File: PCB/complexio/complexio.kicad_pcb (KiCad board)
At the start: 2 copper layers, 1 part, among them U1 STM32F401RETx

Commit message: Initial code,schem & added assets
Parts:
- added BL1: Bluetooth HC-05 module, Connector_PinSocket_2.54mm:PinSocket_1x06_P2.54mm_Vertical, F.Cu at (104.8, 77.9)
- added C1: 100n, Capacitor_SMD:C_0402_1005Metric, F.Cu at (108.5, 76.6)
- added C10: 10u, Capacitor_SMD:C_0603_1608Metric, F.Cu at (128.7, 175.1)
- added C11: 100n, Capacitor_SMD:C_0402_1005Metric, F.Cu at (124.0, 178.5)
- added C12: 1u, Capacitor_SMD:C_0402_1005Metric, F.Cu at (125.9, 178.5)
- added C13: 100n, Capacitor_SMD:C_0402_1005Metric, F.Cu at (127.9, 178.5)
- added C14: 1u, Capacitor_SMD:C_0402_1005Metric, F.Cu at (129.9, 178.5)
- added C15: 100n, Capacitor_SMD:C_0402_1005Metric, F.Cu at (131.8, 178.5)
- added C16: 1u, Capacitor_SMD:C_0402_1005Metric, F.Cu at (133.8, 178.5)
- added C2: 100n, Capacitor_SMD:C_0402_1005Metric, F.Cu at (108.5, 78.6)
- added C3: 100n, Capacitor_SMD:C_0402_1005Metric, F.Cu at (108.5, 80.5)
- added C4: 100n, Capacitor_SMD:C_0402_1005Metric, F.Cu at (108.5, 82.5)
- added C5: 10u, Capacitor_SMD:C_0603_1608Metric, F.Cu at (112.0, 88.2)
- added C6: 10n, Capacitor_SMD:C_0402_1005Metric, F.Cu at (108.5, 84.5)
- added C7: 1u, Capacitor_SMD:C_0402_1005Metric, F.Cu at (108.5, 86.5)
- added C8: 1u, Capacitor_SMD:C_0402_1005Metric, F.Cu at (108.5, 88.4)
- added C9: 100n, Capacitor_SMD:C_0402_1005Metric, F.Cu at (108.5, 90.4)
- added FB1: 120R, Inductor_SMD:L_0603_1608Metric, F.Cu at (112.0, 90.7)
- added IMU1: MPU6050, MPU6050:MPU6050, F.Cu at (89.6, 58.2)
- added J3: Conn_01x12_Pin, Connector_PinHeader_2.54mm:PinHeader_1x12_P2.54mm_Horizontal, F.Cu at (107.4, 147.0)
- added OLED1: SPI OLED Screen 128x64 pixels, Connector_PinSocket_2.54mm:PinSocket_1x07_P2.54mm_Vertical, F.Cu at (104.8, 58.1)
- added Q1: AO3400A, Package_TO_SOT_SMD:SOT-23, F.Cu at (125.2, 174.6)
- added R1: 10k, Resistor_SMD:R_0402_1005Metric, F.Cu at (115.4, 88.0)
- added R10: 47k, Resistor_SMD:R_0402_1005Metric, F.Cu at (116.0, 175.6)
- added R11: 47k, Resistor_SMD:R_0402_1005Metric, F.Cu at (118.0, 175.6)
- added R12: 47, Resistor_SMD:R_0402_1005Metric, F.Cu at (120.0, 175.6)
- added R13: 47, Resistor_SMD:R_0402_1005Metric, F.Cu at (122.0, 175.6)
- added R14: 47k, Resistor_SMD:R_0402_1005Metric, F.Cu at (112.0, 172.7)
- added R15: 47k, Resistor_SMD:R_0402_1005Metric, F.Cu at (114.0, 172.7)
- added R16: 47, Resistor_SMD:R_0402_1005Metric, F.Cu at (116.0, 172.7)
- added R2: 47k, Resistor_SMD:R_0402_1005Metric, F.Cu at (112.0, 178.5)
- added R3: 47k, Resistor_SMD:R_0402_1005Metric, F.Cu at (114.0, 178.5)
- added R4: 47k, Resistor_SMD:R_0402_1005Metric, F.Cu at (116.0, 178.5)
- added R5: 47, Resistor_SMD:R_0402_1005Metric, F.Cu at (118.0, 178.5)
- added R6: 47k, Resistor_SMD:R_0402_1005Metric, F.Cu at (120.0, 178.5)
- added R7: 47k, Resistor_SMD:R_0402_1005Metric, F.Cu at (122.0, 178.5)
- added R8: 47, Resistor_SMD:R_0402_1005Metric, F.Cu at (112.0, 175.6)
- added R9: 47k, Resistor_SMD:R_0402_1005Metric, F.Cu at (114.0, 175.6)
- added SW1: SW_SPDT, Button_Switch_THT:SW_E-Switch_EG1224_SPDT_Angled, F.Cu at (110.9, 59.4)
- added U10: KTIR0711S, KTIR0711S:KTIR0711S, F.Cu at (114.2, 163.9)
- added U11: KTIR0711S, KTIR0711S:KTIR0711S, F.Cu at (119.1, 163.9)
- added U12: KTIR0711S, KTIR0711S:KTIR0711S, F.Cu at (124.0, 163.9)
- added U2: TB6612FNG, Package_SO:SSOP-24_5.3x8.2mm_P0.65mm, F.Cu at (97.2, 60.8)
- added U3: TB6612FNG, Package_SO:SSOP-24_5.3x8.2mm_P0.65mm, F.Cu at (97.2, 70.8)
- added U4: KTIR0711S, KTIR0711S:KTIR0711S, F.Cu at (114.2, 152.1)
- added U5: KTIR0711S, KTIR0711S:KTIR0711S, F.Cu at (119.1, 152.1)
- added U6: KTIR0711S, KTIR0711S:KTIR0711S, F.Cu at (124.0, 152.1)
- added U7: KTIR0711S, KTIR0711S:KTIR0711S, F.Cu at (114.2, 158.0)
- added U8: KTIR0711S, KTIR0711S:KTIR0711S, F.Cu at (119.1, 158.0)
- added U9: KTIR0711S, KTIR0711S:KTIR0711S, F.Cu at (124.0, 158.0)
- U1: value STM32F401RETx -> STM32F103C8T6; footprint Package_QFP:LQFP-64_10x10mm_P0.5mm -> Package_QFP:LQFP-48_7x7mm_P0.5mm
- moved U1 30.1 mm to (115.6, 81.3)
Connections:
- U1 pad 1: unconnected-(U1-VBAT-Pad1) -> +3V3
- U1 pad 18: Net-(U1-VSS-Pad18) -> unconnected-(U1-PB0-Pad18)
- U1 pad 23: unconnected-(U1-PA7-Pad23) -> GND
- U1 pad 24: unconnected-(U1-PC4-Pad24) -> +3V3
- U1 pad 31: Net-(U1-VSS-Pad18) -> unconnected-(U1-PA10-Pad31)
- U1 pad 35: unconnected-(U1-PB14-Pad35) -> GND
- U1 pad 36: unconnected-(U1-PB15-Pad36) -> +3V3
- U1 pad 44: unconnected-(U1-PA11-Pad44) -> /BOOT0
- U1 pad 47: Net-(U1-VSS-Pad18) -> GND
- U1 pad 48: unconnected-(U1-VDD-Pad48) -> +3V3
- U1 pad 7: unconnected-(U1-NRST-Pad7) -> /NRST
- U1 pad 8: unconnected-(U1-PC0-Pad8) -> GND
- U1 pad 9: unconnected-(U1-PC1-Pad9) -> +3.3VA
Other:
- board outline added: 69 x 130 mm

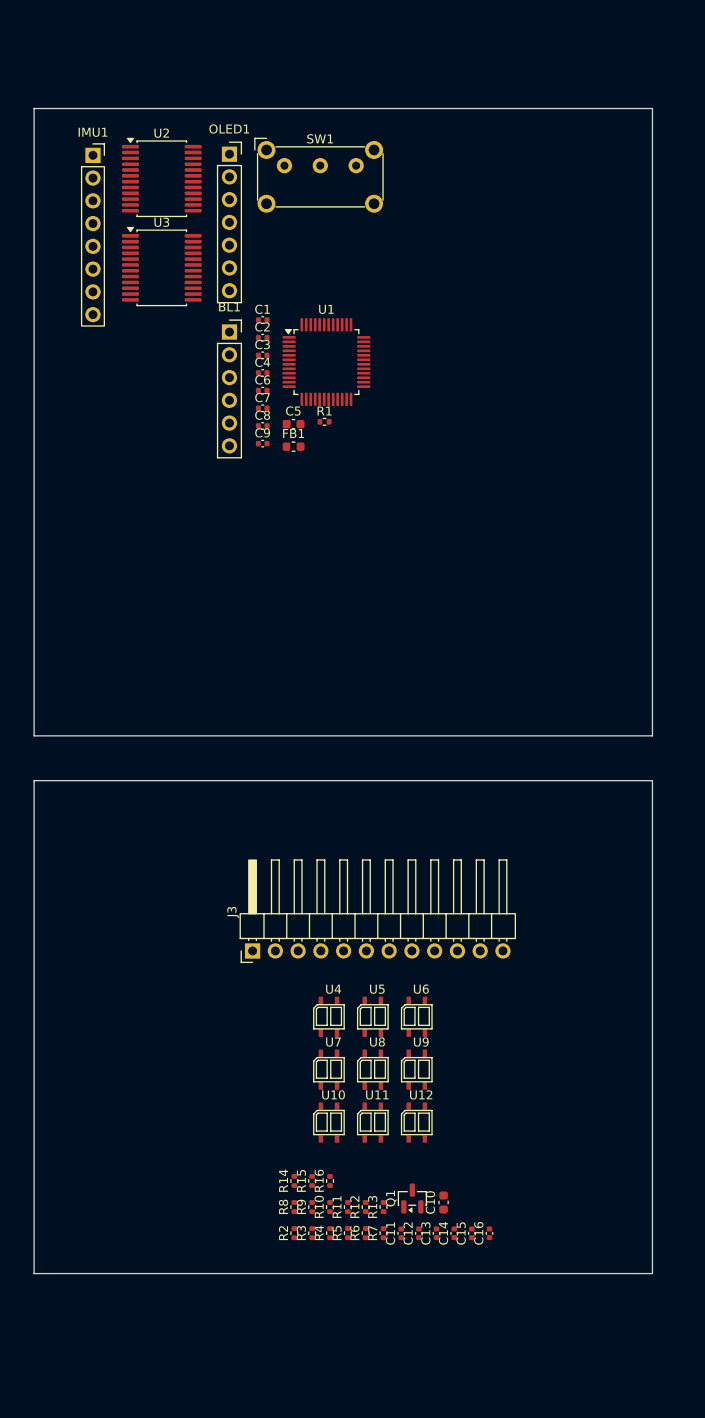
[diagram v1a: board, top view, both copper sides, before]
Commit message: Sensor array finished & main schem modified
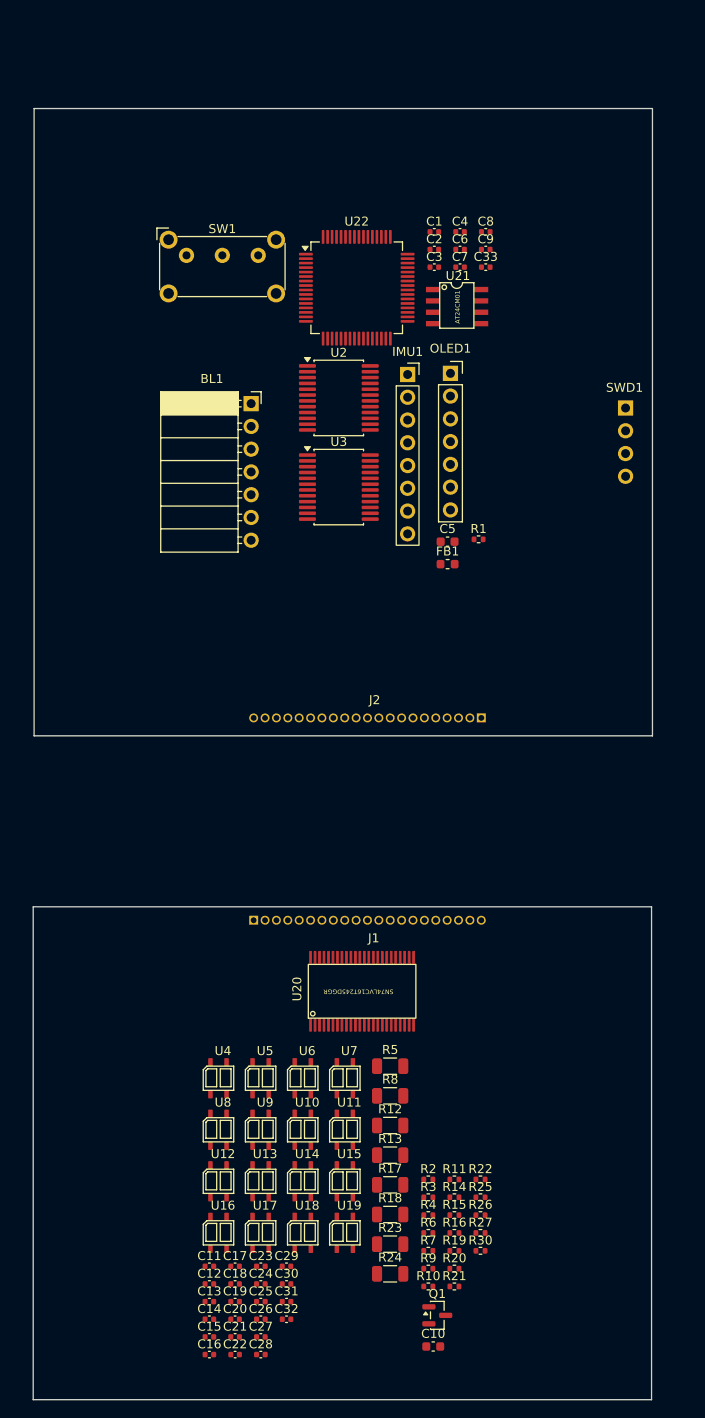
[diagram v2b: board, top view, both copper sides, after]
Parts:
- removed J3: Conn_01x12_Pin, Connector_PinHeader_2.54mm:PinHeader_1x12_P2.54mm_Horizontal
- removed U1: STM32F103C8T6, Package_QFP:LQFP-48_7x7mm_P0.5mm
- added C17: 100n, Capacitor_SMD:C_0402_1005Metric, F.Cu at (105.4, 182.2)
- added C18: 1u, Capacitor_SMD:C_0402_1005Metric, F.Cu at (105.4, 184.2)
- added C19: 100n, Capacitor_SMD:C_0402_1005Metric, F.Cu at (105.4, 186.1)
- added C20: 1u, Capacitor_SMD:C_0402_1005Metric, F.Cu at (105.4, 188.1)
- added C21: 100n, Capacitor_SMD:C_0402_1005Metric, F.Cu at (105.4, 190.1)
- added C22: 1u, Capacitor_SMD:C_0402_1005Metric, F.Cu at (105.4, 192.0)
- added C23: 100n, Capacitor_SMD:C_0402_1005Metric, F.Cu at (108.3, 182.2)
- added C24: 1u, Capacitor_SMD:C_0402_1005Metric, F.Cu at (108.3, 184.2)
- added C25: 100n, Capacitor_SMD:C_0402_1005Metric, F.Cu at (108.3, 186.1)
- added C26: 1u, Capacitor_SMD:C_0402_1005Metric, F.Cu at (108.3, 188.1)
- added C27: 100n, Capacitor_SMD:C_0402_1005Metric, F.Cu at (108.3, 190.1)
- added C28: 100n, Capacitor_SMD:C_0402_1005Metric, F.Cu at (108.3, 192.0)
- added C29: 1u, Capacitor_SMD:C_0402_1005Metric, F.Cu at (111.2, 182.2)
- added C30: 100n, Capacitor_SMD:C_0402_1005Metric, F.Cu at (111.2, 184.2)
- added C31: 100n, Capacitor_SMD:C_0402_1005Metric, F.Cu at (111.2, 186.1)
- added C32: 1u, Capacitor_SMD:C_0402_1005Metric, F.Cu at (111.2, 188.1)
- added C33: 100n, Capacitor_SMD:C_0402_1005Metric, F.Cu at (133.4, 70.7)
- added J1: Conn_01x21_Pin, Connector_PinHeader_1.27mm:PinHeader_1x21_P1.27mm_Horizontal, F.Cu at (107.5, 143.6)
- added J2: Conn_01x21_Pin, Connector_PinHeader_1.27mm:PinHeader_1x21_P1.27mm_Horizontal, F.Cu at (132.9, 121.0)
- added R17: 47, Resistor_SMD:R_1206_3216Metric, F.Cu at (122.7, 173.1)
- added R18: 47, Resistor_SMD:R_1206_3216Metric, F.Cu at (122.7, 176.4)
- added R19: 47k, Resistor_SMD:R_0402_1005Metric, F.Cu at (129.9, 180.5)
- added R20: 47k, Resistor_SMD:R_0402_1005Metric, F.Cu at (129.9, 182.4)
- added R21: 47k, Resistor_SMD:R_0402_1005Metric, F.Cu at (129.9, 184.4)
- added R22: 47k, Resistor_SMD:R_0402_1005Metric, F.Cu at (132.8, 172.5)
- added R23: 47, Resistor_SMD:R_1206_3216Metric, F.Cu at (122.7, 179.7)
- added R24: 47, Resistor_SMD:R_1206_3216Metric, F.Cu at (122.7, 183.0)
- added R25: 47k, Resistor_SMD:R_0402_1005Metric, F.Cu at (132.8, 174.5)
- added R26: 47k, Resistor_SMD:R_0402_1005Metric, F.Cu at (132.8, 176.5)
- added R27: 10k, Resistor_SMD:R_0402_1005Metric, F.Cu at (132.8, 178.5)
- added R30: 10k, Resistor_SMD:R_0402_1005Metric, F.Cu at (132.8, 180.5)
- added SWD1: Serial Wire Debug Interface connector, Connector_PinHeader_2.54mm:PinHeader_1x04_P2.54mm_Horizontal, F.Cu at (149.0, 86.4)
- added U13: KTIR0711S, KTIR0711S:KTIR0711S, F.Cu at (106.6, 170.5)
- added U14: KTIR0711S, KTIR0711S:KTIR0711S, F.Cu at (111.3, 170.5)
- added U15: KTIR0711S, KTIR0711S:KTIR0711S, F.Cu at (116.0, 170.5)
- added U16: KTIR0711S, KTIR0711S:KTIR0711S, F.Cu at (101.9, 176.2)
- added U17: KTIR0711S, KTIR0711S:KTIR0711S, F.Cu at (106.6, 176.2)
- added U18: KTIR0711S, KTIR0711S:KTIR0711S, F.Cu at (111.3, 176.2)
- added U19: KTIR0711S, KTIR0711S:KTIR0711S, F.Cu at (116.0, 176.2)
- added U20: SN74LVC16T245DGGR, SN74LVC16T245DGGR:SN74LVC16T245DGGR, F.Cu at (113.6, 154.5)
- added U21: AT24CM01, AT24CM01:AT24CM01, F.Cu at (128.3, 72.4)
- added U22: STM32F303RBTx, Package_QFP:LQFP-64_10x10mm_P0.5mm, F.Cu at (119.0, 73.0)
- BL1: footprint Connector_PinSocket_2.54mm:PinSocket_1x06_P2.54mm_Vertical -> Connector_PinSocket_2.54mm:PinSocket_1x07_P2.54mm_Horizontal
- R12, R13, R5, R8: footprint Resistor_SMD:R_0402_1005Metric -> Resistor_SMD:R_1206_3216Metric
- R16: value 47 -> 47k
- moved IMU1 42.8 mm to (124.7, 82.7)
- moved OLED1 34.7 mm to (129.5, 82.5)
- moved C16 34.1 mm to (102.6, 192.0), turned to 0 degrees
- moved C8 33.0 mm to (133.4, 66.8)
- moved C9 33.0 mm to (133.4, 68.7)
- moved C15 31.5 mm to (102.6, 190.1), turned to 0 degrees
- moved U2 31.4 mm to (117.0, 85.3)
- moved U3 31.4 mm to (117.0, 95.2)
- moved C14 29.0 mm to (102.6, 188.1), turned to 0 degrees
- moved C4 27.1 mm to (130.5, 66.8)
- moved C6 27.1 mm to (130.5, 68.7)
- moved C7 27.1 mm to (130.5, 70.7)
- moved C13 26.5 mm to (102.6, 186.1), turned to 0 degrees
- moved C12 24.1 mm to (102.6, 184.2), turned to 0 degrees
- moved U12 23.1 mm to (101.9, 170.5)
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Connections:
- net LEDON renamed /Sensor_array/ledon
- net OUT1 renamed /Sensor_array/OUT1
- net OUT2 renamed /Sensor_array/OUT2
- net OUT3 renamed Net-(U6-collector)
- net OUT4 renamed /Sensor_array/OUT4
- net OUT5 renamed /Sensor_array/OUT9
- net OUT6 renamed /Sensor_array/OUT10
- net OUT7 renamed Net-(U10-collector)
- net OUT8 renamed /Sensor_array/OUT12
- net OUT9 renamed /Sensor_array/OUT5
- C10 pad 1: VCC -> +5V
- C11 pad 1: VCC -> +5V
- C12 pad 1: VCC -> +5V
- C13 pad 1: VCC -> +5V
- C14 pad 1: VCC -> +5V
- C15 pad 1: VCC -> +5V
- C16 pad 1: VCC -> +5V
- R10 pad 2: VCC -> +5V
- R11 pad 2: VCC -> +5V
- R12 pad 1: Net-(U4-anode) -> +5V
- R12 pad 2: VCC -> Net-(U6-anode)
- R13 pad 1: Net-(U10-anode) -> +5V
- R13 pad 2: VCC -> Net-(U10-anode)
- R14 pad 2: VCC -> +5V
- R15 pad 2: VCC -> +5V
- R16 pad 1: Net-(U12-anode) -> /Sensor_array/OUT13
- R16 pad 2: VCC -> +5V
- R2 pad 2: VCC -> +5V
- R3 pad 2: VCC -> +5V
- R4 pad 2: VCC -> +5V
- R5 pad 1: Net-(U6-anode) -> +5V
- R5 pad 2: VCC -> Net-(U4-anode)
- R6 pad 2: VCC -> +5V
- R7 pad 2: VCC -> +5V
- R8 pad 1: Net-(U8-anode) -> +5V
- R8 pad 2: VCC -> Net-(U8-anode)
- R9 pad 2: VCC -> +5V
- U12 pad 4: /Sensor_array/LED_Cathode -> Net-(U12-cathode)
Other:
- board size 69 x 130 mm -> 69.1 x 144.1 mm

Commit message: Changed firmware & SMD of mpu6050+minor changes
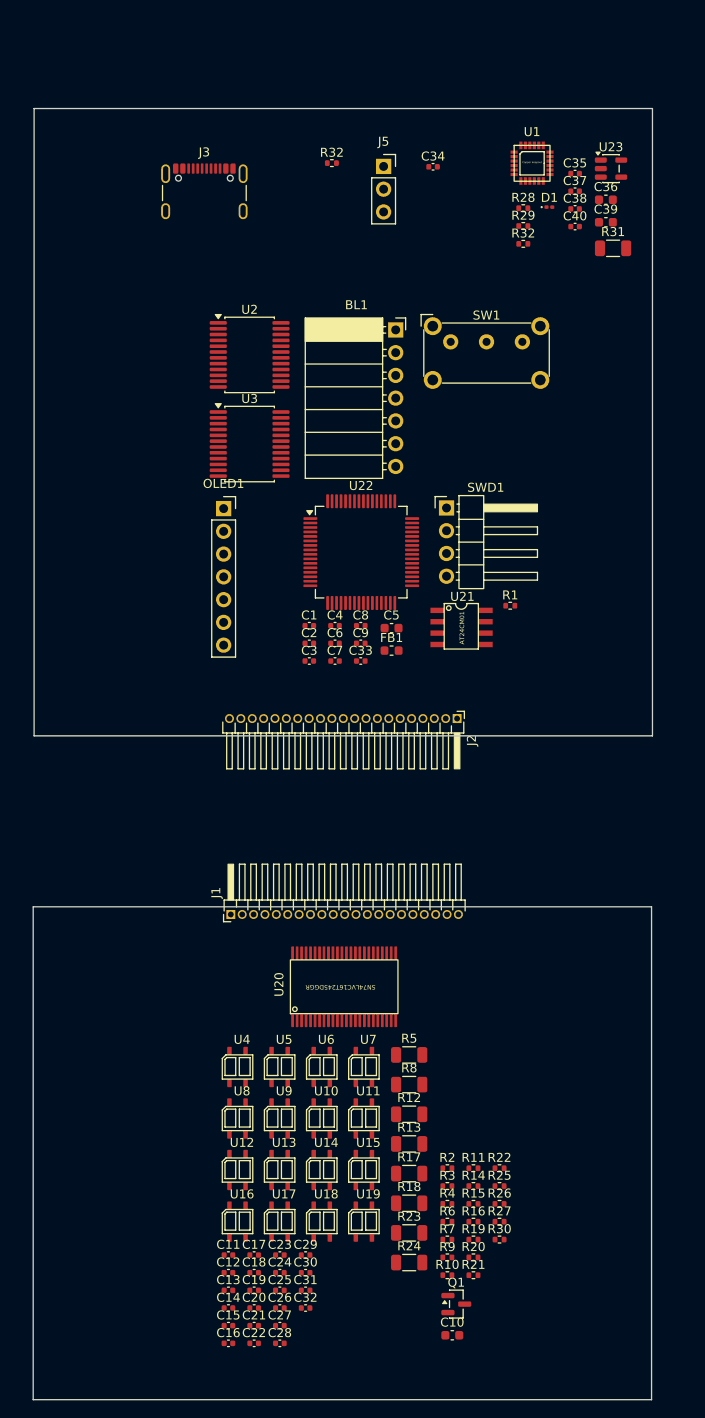
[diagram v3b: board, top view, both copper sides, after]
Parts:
- removed IMU1: MPU6050, MPU6050:MPU6050
- added C34: 2n2, Capacitor_SMD:C_0402_1005Metric, F.Cu at (127.5, 59.5)
- added C35: 100n, Capacitor_SMD:C_0402_1005Metric, F.Cu at (143.4, 60.3)
- added C36: 4u7, Capacitor_SMD:C_0603_1608Metric, F.Cu at (146.8, 63.2)
- added C37: 10n, Capacitor_SMD:C_0402_1005Metric, F.Cu at (143.4, 62.2)
- added C38: 100n, Capacitor_SMD:C_0402_1005Metric, F.Cu at (143.4, 64.2)
- added C39: 10u, Capacitor_SMD:C_0603_1608Metric, F.Cu at (146.8, 65.7)
- added C40: 100n, Capacitor_SMD:C_0402_1005Metric, F.Cu at (143.4, 66.2)
- added D1: LED, LED_SMD:LED_0201_0603Metric, F.Cu at (140.5, 64.0)
- added J3: USB_C_Receptacle_USB2.0_16P, Connector_USB:USB_C_Receptacle_GCT_USB4105-xx-A_16P_TopMnt_Horizontal, F.Cu at (102.0, 63.4)
- added J5: Conn_01x03_Pin, Connector_PinSocket_2.54mm:PinSocket_1x03_P2.54mm_Vertical, F.Cu at (122.0, 59.5)
- added R28: 4k7, Resistor_SMD:R_0402_1005Metric, F.Cu at (137.6, 64.1)
- added R29: 4k7, Resistor_SMD:R_0402_1005Metric, F.Cu at (137.6, 66.1)
- added R31: 1k, Resistor_SMD:R_1206_3216Metric, F.Cu at (147.6, 68.6)
- added R32: 4k7, Resistor_SMD:R_0402_1005Metric, F.Cu at (116.2, 59.1)
- added R32: 4k7, Resistor_SMD:R_0402_1005Metric, F.Cu at (137.6, 68.1)
- added U1: MPU6050, MPU6050:MPU6050SMD, F.Cu at (136.6, 57.1)
- added U23: AP2112K-3.3, Package_TO_SOT_SMD:SOT-23-5, F.Cu at (147.4, 59.7)
- U22: value STM32F303RBTx -> STM32F303RBT6
- moved C2 46.1 mm to (113.7, 112.7)
- moved C3 46.1 mm to (113.7, 114.7)
- moved C33 46.1 mm to (119.5, 114.7)
- moved C6 46.1 mm to (116.6, 112.7)
- moved C7 46.1 mm to (116.6, 114.7)
- moved C9 46.1 mm to (119.5, 112.7)
- moved C1 46.1 mm to (113.7, 110.7)
- moved C4 46.1 mm to (116.6, 110.7)
- moved C8 46.1 mm to (119.5, 110.7)
- moved U21 35.8 mm to (128.8, 108.2)
- moved SW1 31.0 mm to (129.5, 79.0)
- moved U22 29.5 mm to (119.5, 102.5)
- moved OLED1 29.5 mm to (104.2, 97.6)
- moved SWD1 22.9 mm to (129.0, 97.6)
- moved BL1 18.1 mm to (123.3, 77.7)
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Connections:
- C26 pad 1: unconnected-(C26-Pad1) -> +5V
- C26 pad 2: unconnected-(C26-Pad2) -> GND
- J2 pad 1: /sen16 -> /Sensor_array/sen16
- J2 pad 10: /sen7 -> /Sensor_array/sen7
- J2 pad 11: /sen6 -> /Sensor_array/sen6
- J2 pad 12: /sen5 -> /Sensor_array/sen5
- J2 pad 13: /sen4 -> /Sensor_array/sen4
- J2 pad 14: /sen3 -> /Sensor_array/sen3
- J2 pad 15: /sen2 -> /Sensor_array/sen2
- J2 pad 16: /sen1 -> /Sensor_array/sen1
- J2 pad 17: /ledon -> /Sensor_array/ledon
- J2 pad 18: /oe -> /Sensor_array/oe
- J2 pad 2: /sen15 -> /Sensor_array/sen15
- J2 pad 3: /sen14 -> /Sensor_array/sen14
- J2 pad 4: /sen13 -> /Sensor_array/sen13
- J2 pad 5: /sen12 -> /Sensor_array/sen12
- J2 pad 6: /sen11 -> /Sensor_array/sen11
- J2 pad 7: /sen10 -> /Sensor_array/sen10
- J2 pad 8: /sen9 -> /Sensor_array/sen9
- J2 pad 9: /sen8 -> /Sensor_array/sen8
- R10 pad 1: Net-(U10-collector) -> /Sensor_array/OUT11
- R21 pad 1: Net-(U16-collector) -> /Sensor_array/OUT7
- R22 pad 1: Net-(U17-collector) -> /Sensor_array/OUT15
- R4 pad 1: Net-(U6-collector) -> /Sensor_array/OUT3
- SWD1 pad 1: unconnected-(SWD1-SWDIO-Pad1) -> /PA13
- SWD1 pad 2: unconnected-(SWD1-GND-Pad2) -> GND
- SWD1 pad 3: unconnected-(SWD1-SWCLK-Pad3) -> /PA14
- SWD1 pad 4: unconnected-(SWD1-3V3-Pad4) -> +3V3
- U10 pad 3: Net-(U10-collector) -> /Sensor_array/OUT11
- U16 pad 3: Net-(U16-collector) -> /Sensor_array/OUT7
- U17 pad 3: Net-(U17-collector) -> /Sensor_array/OUT15
- U22 pad 46: unconnected-(U22-PA13-Pad46) -> /PA13
- U22 pad 49: unconnected-(U22-PA14-Pad49) -> /PA14
- U22 pad 50: unconnected-(U22-PA15-Pad50) -> /PA15
- U6 pad 3: Net-(U6-collector) -> /Sensor_array/OUT3
